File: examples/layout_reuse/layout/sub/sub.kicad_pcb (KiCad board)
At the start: 2 copper layers, 3 parts

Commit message: partialy fix simple val repr
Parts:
- R1, R2, R3: value {1000.0±1.0%}Ω -> 1000.0Ω
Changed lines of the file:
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@@
 			)
 		)
-		(property "Value" "{1000.0±1.0%}Ω"
+		(property "Value" "1000.0Ω"
 			(at 0 4)
 			(layer "F.Fab")
@@
 			(hide yes)
 		)
-		(property "resistance" "{1000.0±1.0%}Ω"
+		(property "resistance" "1000.0±1.0%Ω"
 			(at 0 0 0)
 			(layer "User.9")
@@
 			(hide yes)
 		)
-		(property "PARAM_resistance" "{\"type\": \"Quantity_Interval_Disjoint\", \"data\": {\"intervals\": {\"type\": \"Numeric_Interval_Disjoint\", \"data\": {\"intervals\": [{\"type\": \"Numeric_Interval\", \"data\": {\"min\": 990.0000002235174, \"max\": 1009.9999997764826}}]}}, \"unit\": \"\u03a9\"}}"
+		(property "PARAM_resistance" "{\"type\": \"Quantity_Interval_Disjoint\", \"data\": {\"intervals\": {\"type\": \"Numeric_Interval_Disjoint\", \"data\": {\"intervals\": [{\"type\": \"Numeric_Interval\", \"data\": {\"min\": 990.0000002235174, \"max\": 1009.9999997764826}}]}}, \"unit\": \"Ω\"}}"
 			(at 0 0 0)
 			(layer "User.9")
@@
 			)
 		)
-		(property "Value" "{1000.0±1.0%}Ω"
+		(property "Value" "1000.0Ω"
 			(at 0 4)
 			(layer "F.Fab")
@@
 			(hide yes)
 		)
-		(property "resistance" "{1000.0±1.0%}Ω"
+		(property "resistance" "1000.0±1.0%Ω"
 			(at 0 0 0)
 			(layer "User.9")
@@
 			(hide yes)
 		)
-		(property "PARAM_resistance" "{\"type\": \"Quantity_Interval_Disjoint\", \"data\": {\"intervals\": {\"type\": \"Numeric_Interval_Disjoint\", \"data\": {\"intervals\": [{\"type\": \"Numeric_Interval\", \"data\": {\"min\": 990.0000002235174, \"max\": 1009.9999997764826}}]}}, \"unit\": \"\u03a9\"}}"
+		(property "PARAM_resistance" "{\"type\": \"Quantity_Interval_Disjoint\", \"data\": {\"intervals\": {\"type\": \"Numeric_Interval_Disjoint\", \"data\": {\"intervals\": [{\"type\": \"Numeric_Interval\", \"data\": {\"min\": 990.0000002235174, \"max\": 1009.9999997764826}}]}}, \"unit\": \"Ω\"}}"
 			(at 0 0 0)
 			(layer "User.9")
@@
 			)
 		)
-		(property "Value" "{1000.0±1.0%}Ω"
+		(property "Value" "1000.0Ω"
 			(at 0 4)
 			(layer "F.Fab")
@@
 			(hide yes)
 		)
-		(property "resistance" "{1000.0±1.0%}Ω"
+		(property "resistance" "1000.0±1.0%Ω"
 			(at 0 0 0)
 			(layer "User.9")
@@
 			(hide yes)
 		)
-		(property "PARAM_resistance" "{\"type\": \"Quantity_Interval_Disjoint\", \"data\": {\"intervals\": {\"type\": \"Numeric_Interval_Disjoint\", \"data\": {\"intervals\": [{\"type\": \"Numeric_Interval\", \"data\": {\"min\": 990.0000002235174, \"max\": 1009.9999997764826}}]}}, \"unit\": \"\u03a9\"}}"
-			(at 0 0 0)
-			(layer "User.9")
+		(property "PARAM_resistance" "{\"type\": \"Quantity_Interval_Disjoint\", \"data\": {\"intervals\": {\"type\": \"Numeric_Interval_Disjoint\", \"data\": {\"intervals\": [{\"type\": \"Numeric_Interval\", \"data\": {\"min\": 990.0000002235174, \"max\": 1009.9999997764826}}]}}, \"unit\": \"Ω\"}}"
+			(at 0 0 0)
+			(layer "User.9")

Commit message: add builid
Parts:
- R1, R2, R3: value 1000.0Ω -> 1kΩ
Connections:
- net r_chain[0].unnamed[0]-unnamed[0] renamed unnamed[0]
- R1 pad 2: unnamed[0]-0 -> unnamed[0]-1
- R2 pad 1: unnamed[0]-0 -> unnamed[0]-1
- R2 pad 2: unnamed[0]-1 -> unnamed[0]-2
- R3 pad 1: unnamed[0]-1 -> unnamed[0]-2
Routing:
- net unnamed[0]-2: track 0.00 -> 1.57 mm
- net unnamed[0]-1: track 1.57 -> 0.00 mm
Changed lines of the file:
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@@
 			(usegerberadvancedattributes yes)
 			(creategerberjobfile yes)
-			(dashed_line_dash_ratio 12.000000)
-			(dashed_line_gap_ratio 3.000000)
+			(dashed_line_dash_ratio 12)
+			(dashed_line_gap_ratio 3)
 			(svgprecision 4)
 			(plotframeref no)
@@
 			(hpglpennumber 1)
 			(hpglpenspeed 20)
-			(hpglpendiameter 15.000000)
+			(hpglpendiameter 15)
 			(pdf_front_fp_property_popups yes)
 			(pdf_back_fp_property_popups yes)
@@
 	)
 	(net 1 "unnamed[1]")
-	(net 2 "unnamed[0]-1")
-	(net 3 "unnamed[0]-0")
-	(net 4 "r_chain[0].unnamed[0]-unnamed[0]")
+	(net 2 "unnamed[0]-2")
+	(net 3 "unnamed[0]-1")
+	(net 4 "unnamed[0]")
 	(footprint "UNI_ROYAL_0402WGF1001TCE:R0402"
 		(layer "F.Cu")
@@
 			)
 		)
-		(property "Value" "1000.0Ω"
+		(property "Value" "1kΩ"
 			(at 0 4)
 			(layer "F.Fab")
@@
 			(hide yes)
 		)
-		(property "resistance" "1000.0±1.0%Ω"
-			(at 0 0 0)
-			(layer "User.9")
-			(hide yes)
-		)
-		(property "max_power" "0.0625W"
-			(at 0 0 0)
-			(layer "User.9")
-			(hide yes)
-		)
-		(property "max_voltage" "50.0V"
+		(property "resistance" "1±20.0%kΩ"
+			(at 0 0 0)
+			(layer "User.9")
+			(hide yes)
+		)
+		(property "max_power" "any ≥0W"
+			(at 0 0 0)
+			(layer "User.9")
+			(hide yes)
+		)
+		(property "max_voltage" "any ≥0V"
 			(at 0 0 0)
 			(layer "User.9")
@@
 			(hide yes)
 		)
-		(property "PARAM_max_power" "{\"type\": \"Quantity_Set_Discrete\", \"data\": {\"intervals\": {\"type\": \"Numeric_Interval_Disjoint\", \"data\": {\"intervals\": [{\"type\": \"Numeric_Interval\", \"data\": {\"min\": 0.0625, \"max\": 0.0625}}]}}, \"unit\": \"W\"}}"
-			(at 0 0 0)
-			(layer "User.9")
-			(hide yes)
-		)
-		(property "PARAM_max_voltage" "{\"type\": \"Quantity_Set_Discrete\", \"data\": {\"intervals\": {\"type\": \"Numeric_Interval_Disjoint\", \"data\": {\"intervals\": [{\"type\": \"Numeric_Interval\", \"data\": {\"min\": 50.0, \"max\": 50.0}}]}}, \"unit\": \"V\"}}"
-			(at 0 0 0)
-			(layer "User.9")
-			(hide yes)
-		)
-		(property "PARAM_resistance" "{\"type\": \"Quantity_Interval_Disjoint\", \"data\": {\"intervals\": {\"type\": \"Numeric_Interval_Disjoint\", \"data\": {\"intervals\": [{\"type\": \"Numeric_Interval\", \"data\": {\"min\": 990.0000002235174, \"max\": 1009.9999997764826}}]}}, \"unit\": \"Ω\"}}"
+		(property "PARAM_max_power" "{\"type\": \"Quantity_Set_Discrete\", \"data\": {\"intervals\": {\"type\": \"Numeric_Interval_Disjoint\", \"data\": {\"intervals\": [{\"type\": \"Numeric_Interval\", \"data\": {\"min\": 0.0625, \"max\": 0.0625}}]}}, \"unit\": \"watt\"}}"
+			(at 0 0 0)
+			(layer "User.9")
+			(hide yes)
+		)
+		(property "PARAM_max_voltage" "{\"type\": \"Quantity_Set_Discrete\", \"data\": {\"intervals\": {\"type\": \"Numeric_Interval_Disjoint\", \"data\": {\"intervals\": [{\"type\": \"Numeric_Interval\", \"data\": {\"min\": 50.0, \"max\": 50.0}}]}}, \"unit\": \"volt\"}}"
+			(at 0 0 0)
+			(layer "User.9")
+			(hide yes)
+		)
+		(property "PARAM_resistance" "{\"type\": \"Quantity_Interval_Disjoint\", \"data\": {\"intervals\": {\"type\": \"Numeric_Interval_Disjoint\", \"data\": {\"intervals\": [{\"type\": \"Numeric_Interval\", \"data\": {\"min\": 990.0000002235174, \"max\": 1009.9999997764826}}]}}, \"unit\": \"ohm\"}}"
 			(at 0 0 0)
 			(layer "User.9")
@@
 			(size 0.57 0.54)
 			(layers "F.Cu" "F.Paste" "F.Mask")
-			(net 3 "unnamed[0]-0")
+			(net 3 "unnamed[0]-1")
 		)
 		(pad "1" smd rect
@@
 			(size 0.57 0.54)
 			(layers "F.Cu" "F.Paste" "F.Mask")
-			(net 4 "r_chain[0].unnamed[0]-unnamed[0]")
+			(net 4 "unnamed[0]")
 		)
 		(embedded_fonts no)
@@
 			)
 		)
-		(property "Value" "1000.0Ω"
+		(property "Value" "1kΩ"
 			(at 0 4)
 			(layer "F.Fab")
@@
 			(hide yes)
 		)
-		(property "resistance" "1000.0±1.0%Ω"
-			(at 0 0 0)
-			(layer "User.9")
-			(hide yes)
-		)
-		(property "max_power" "0.0625W"
-			(at 0 0 0)
-			(layer "User.9")
-			(hide yes)
-		)
-		(property "max_voltage" "50.0V"
+		(property "resistance" "1±20.0%kΩ"
+			(at 0 0 0)
+			(layer "User.9")
+			(hide yes)
+		)
+		(property "max_power" "any ≥0W"
+			(at 0 0 0)
+			(layer "User.9")
+			(hide yes)
+		)
+		(property "max_voltage" "any ≥0V"
 			(at 0 0 0)
 			(layer "User.9")
@@
 			(hide yes)
 		)
-		(property "PARAM_max_power" "{\"type\": \"Quantity_Set_Discrete\", \"data\": {\"intervals\": {\"type\": \"Numeric_Interval_Disjoint\", \"data\": {\"intervals\": [{\"type\": \"Numeric_Interval\", \"data\": {\"min\": 0.0625, \"max\": 0.0625}}]}}, \"unit\": \"W\"}}"
-			(at 0 0 0)
-			(layer "User.9")
-			(hide yes)
-		)
-		(property "PARAM_max_voltage" "{\"type\": \"Quantity_Set_Discrete\", \"data\": {\"intervals\": {\"type\": \"Numeric_Interval_Disjoint\", \"data\": {\"intervals\": [{\"type\": \"Numeric_Interval\", \"data\": {\"min\": 50.0, \"max\": 50.0}}]}}, \"unit\": \"V\"}}"
-			(at 0 0 0)
-			(layer "User.9")
-			(hide yes)
-		)
-		(property "PARAM_resistance" "{\"type\": \"Quantity_Interval_Disjoint\", \"data\": {\"intervals\": {\"type\": \"Numeric_Interval_Disjoint\", \"data\": {\"intervals\": [{\"type\": \"Numeric_Interval\", \"data\": {\"min\": 990.0000002235174, \"max\": 1009.9999997764826}}]}}, \"unit\": \"Ω\"}}"
+		(property "PARAM_max_power" "{\"type\": \"Quantity_Set_Discrete\", \"data\": {\"intervals\": {\"type\": \"Numeric_Interval_Disjoint\", \"data\": {\"intervals\": [{\"type\": \"Numeric_Interval\", \"data\": {\"min\": 0.0625, \"max\": 0.0625}}]}}, \"unit\": \"watt\"}}"
+			(at 0 0 0)
+			(layer "User.9")
+			(hide yes)
+		)
+		(property "PARAM_max_voltage" "{\"type\": \"Quantity_Set_Discrete\", \"data\": {\"intervals\": {\"type\": \"Numeric_Interval_Disjoint\", \"data\": {\"intervals\": [{\"type\": \"Numeric_Interval\", \"data\": {\"min\": 50.0, \"max\": 50.0}}]}}, \"unit\": \"volt\"}}"
+			(at 0 0 0)
+			(layer "User.9")
+			(hide yes)
+		)
+		(property "PARAM_resistance" "{\"type\": \"Quantity_Interval_Disjoint\", \"data\": {\"intervals\": {\"type\": \"Numeric_Interval_Disjoint\", \"data\": {\"intervals\": [{\"type\": \"Numeric_Interval\", \"data\": {\"min\": 990.0000002235174, \"max\": 1009.9999997764826}}]}}, \"unit\": \"ohm\"}}"
 			(at 0 0 0)
 			(layer "User.9")
@@
 			(size 0.57 0.54)
 			(layers "F.Cu" "F.Paste" "F.Mask")
-			(net 2 "unnamed[0]-1")
+			(net 2 "unnamed[0]-2")
 		)
 		(embedded_fonts no)
@@
 			)
 		)
-		(property "Value" "1000.0Ω"
+		(property "Value" "1kΩ"
 			(at 0 4)
 			(layer "F.Fab")
@@
 			(hide yes)
 		)
-		(property "resistance" "1000.0±1.0%Ω"
-			(at 0 0 0)
-			(layer "User.9")
-			(hide yes)
-		)
-		(property "max_power" "0.0625W"
-			(at 0 0 0)
-			(layer "User.9")
-			(hide yes)
-		)
-		(property "max_voltage" "50.0V"
+		(property "resistance" "1±20.0%kΩ"
+			(at 0 0 0)
+			(layer "User.9")
+			(hide yes)
+		)
+		(property "max_power" "any ≥0W"
+			(at 0 0 0)
+			(layer "User.9")
+			(hide yes)
+		)
+		(property "max_voltage" "any ≥0V"
 			(at 0 0 0)
 			(layer "User.9")
@@
 			(hide yes)
 		)
-		(property "PARAM_max_power" "{\"type\": \"Quantity_Set_Discrete\", \"data\": {\"intervals\": {\"type\": \"Numeric_Interval_Disjoint\", \"data\": {\"intervals\": [{\"type\": \"Numeric_Interval\", \"data\": {\"min\": 0.0625, \"max\": 0.0625}}]}}, \"unit\": \"W\"}}"
-			(at 0 0 0)
-			(layer "User.9")
-			(hide yes)
-		)
-		(property "PARAM_max_voltage" "{\"type\": \"Quantity_Set_Discrete\", \"data\": {\"intervals\": {\"type\": \"Numeric_Interval_Disjoint\", \"data\": {\"intervals\": [{\"type\": \"Numeric_Interval\", \"data\": {\"min\": 50.0, \"max\": 50.0}}]}}, \"unit\": \"V\"}}"
-			(at 0 0 0)
-			(layer "User.9")
-			(hide yes)
-		)
-		(property "PARAM_resistance" "{\"type\": \"Quantity_Interval_Disjoint\", \"data\": {\"intervals\": {\"type\": \"Numeric_Interval_Disjoint\", \"data\": {\"intervals\": [{\"type\": \"Numeric_Interval\", \"data\": {\"min\": 990.0000002235174, \"max\": 1009.9999997764826}}]}}, \"unit\": \"Ω\"}}"
+		(property "PARAM_max_power" "{\"type\": \"Quantity_Set_Discrete\", \"data\": {\"intervals\": {\"type\": \"Numeric_Interval_Disjoint\", \"data\": {\"intervals\": [{\"type\": \"Numeric_Interval\", \"data\": {\"min\": 0.0625, \"max\": 0.0625}}]}}, \"unit\": \"watt\"}}"
+			(at 0 0 0)
+			(layer "User.9")
+			(hide yes)
+		)
+		(property "PARAM_max_voltage" "{\"type\": \"Quantity_Set_Discrete\", \"data\": {\"intervals\": {\"type\": \"Numeric_Interval_Disjoint\", \"data\": {\"intervals\": [{\"type\": \"Numeric_Interval\", \"data\": {\"min\": 50.0, \"max\": 50.0}}]}}, \"unit\": \"volt\"}}"
+			(at 0 0 0)
+			(layer "User.9")
+			(hide yes)
+		)
+		(property "PARAM_resistance" "{\"type\": \"Quantity_Interval_Disjoint\", \"data\": {\"intervals\": {\"type\": \"Numeric_Interval_Disjoint\", \"data\": {\"intervals\": [{\"type\": \"Numeric_Interval\", \"data\": {\"min\": 990.0000002235174, \"max\": 1009.9999997764826}}]}}, \"unit\": \"ohm\"}}"
 			(at 0 0 0)
 			(layer "User.9")
@@
 			(size 0.57 0.54)
 			(layers "F.Cu" "F.Paste" "F.Mask")
-			(net 2 "unnamed[0]-1")
+			(net 2 "unnamed[0]-2")
 		)
 		(pad "1" smd rect
@@
 			(size 0.57 0.54)
 			(layers "F.Cu" "F.Paste" "F.Mask")
-			(net 3 "unnamed[0]-0")
+			(net 3 "unnamed[0]-1")
 		)
 		(embedded_fonts no)

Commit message: update layout_reuse layout and parts
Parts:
- R1, R2, R3: value 1kΩ -> 1000Ω
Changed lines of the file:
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@@
 	)
 	(setup
+		(stackup
+			(layer "F.SilkS"
+				(type "Top Silk Screen")
+			)
+			(layer "F.Paste"
+				(type "Top Solder Paste")
+			)
+			(layer "F.Mask"
+				(type "Top Solder Mask")
+				(color "Black")
+				(thickness 0.01)
+				(material "Solder mask")
+				(epsilon_r 3.3)
+			)
+			(layer "F.Cu"
+				(type "copper")
+				(thickness 0.035)
+			)
+			(layer "dielectric 1"
+				(type "core")
+				(thickness 1.51)
+				(material "FR4")
+				(epsilon_r 4.5)
+				(loss_tangent 0.02)
+			)
+			(layer "B.Cu"
+				(type "copper")
+				(thickness 0.035)
+			)
+			(layer "B.Mask"
+				(type "Bottom Solder Mask")
+				(color "Black")
+				(thickness 0.01)
+				(material "Solder mask")
+				(epsilon_r 3.3)
+			)
+			(layer "B.Paste"
+				(type "Bottom Solder Paste")
+			)
+			(layer "B.SilkS"
+				(type "Bottom Silk Screen")
+			)
+			(copper_finish "ENIG")
+		)
 		(pad_to_mask_clearance 0)
 		(allow_soldermask_bridges_in_footprints no)
@@
 			)
 		)
-		(property "Value" "1kΩ"
+		(property "Value" "1000Ω"
 			(at 0 4)
 			(layer "F.Fab")
@@
 			(hide yes)
 		)
-		(property "resistance" "1±20.0%kΩ"
-			(at 0 0 0)
-			(layer "User.9")
-			(hide yes)
-		)
-		(property "max_power" "any ≥0W"
-			(at 0 0 0)
-			(layer "User.9")
-			(hide yes)
-		)
-		(property "max_voltage" "any ≥0V"
+		(property "resistance" "1000±1.0%Ω"
+			(at 0 0 0)
+			(layer "User.9")
+			(hide yes)
+		)
+		(property "max_power" "0.062W"
+			(at 0 0 0)
+			(layer "User.9")
+			(hide yes)
+		)
+		(property "max_voltage" "50V"
 			(at 0 0 0)
 			(layer "User.9")
@@
 			)
 		)
-		(property "Value" "1kΩ"
+		(property "Value" "1000Ω"
 			(at 0 4)
 			(layer "F.Fab")
@@
 			(hide yes)
 		)
-		(property "resistance" "1±20.0%kΩ"
-			(at 0 0 0)
-			(layer "User.9")
-			(hide yes)
-		)
-		(property "max_power" "any ≥0W"
-			(at 0 0 0)
-			(layer "User.9")
-			(hide yes)
-		)
-		(property "max_voltage" "any ≥0V"
+		(property "resistance" "1000±1.0%Ω"
+			(at 0 0 0)
+			(layer "User.9")
+			(hide yes)
+		)
+		(property "max_power" "0.062W"
+			(at 0 0 0)
+			(layer "User.9")
+			(hide yes)
+		)
+		(property "max_voltage" "50V"
 			(at 0 0 0)
 			(layer "User.9")
@@
 			)
 		)
-		(property "Value" "1kΩ"
+		(property "Value" "1000Ω"
 			(at 0 4)
 			(layer "F.Fab")
@@
 			(hide yes)
 		)
-		(property "resistance" "1±20.0%kΩ"
-			(at 0 0 0)
-			(layer "User.9")
-			(hide yes)
-		)
-		(property "max_power" "any ≥0W"
-			(at 0 0 0)
-			(layer "User.9")
-			(hide yes)
-		)
-		(property "max_voltage" "any ≥0V"
-			(at 0 0 0)
-			(layer "User.9")
+		(property "resistance" "1000±1.0%Ω"
+			(at 0 0 0)
+			(layer "User.9")
+			(hide yes)
+		)
+		(property "max_power" "0.062W"
+			(at 0 0 0)
+			(layer "User.9")
+			(hide yes)
+		)
+		(property "max_voltage" "50V"
+			(at 0 0 0)
+			(layer "User.9")

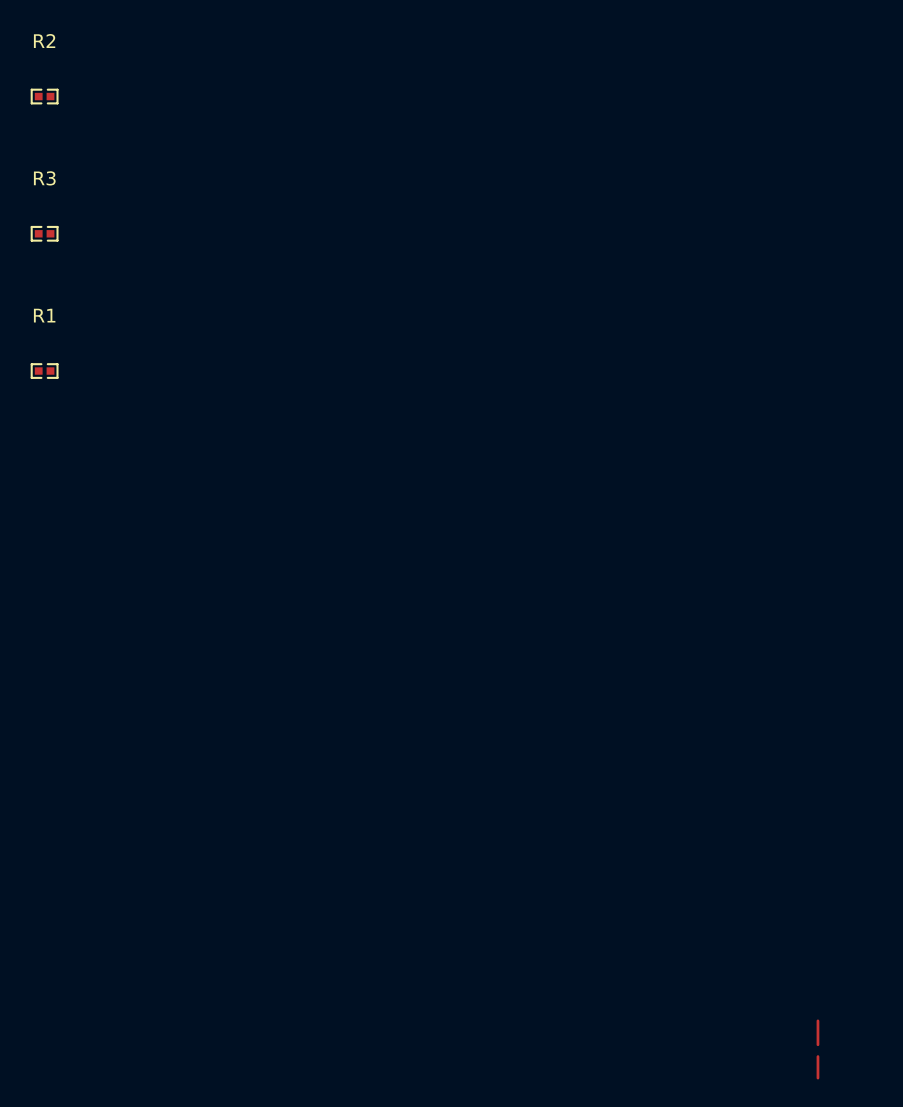
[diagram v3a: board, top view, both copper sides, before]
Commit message: Examples: update examples (#1769)
- simpler I2C example
- fix led badge builds
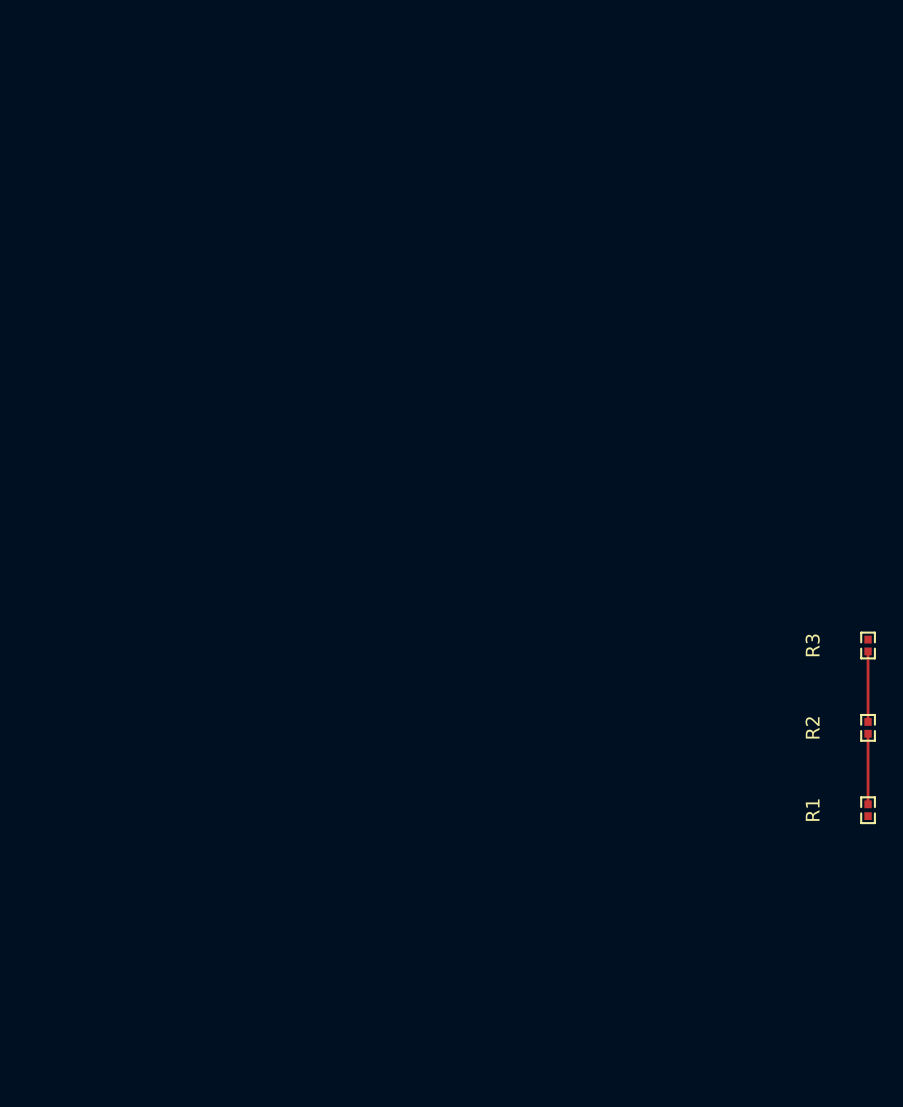
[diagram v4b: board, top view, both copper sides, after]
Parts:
- R1, R2, R3: value 1000Ω -> 1kΩ
- moved R2 75.6 mm to (60.0, 26.0), turned to 90 degrees
- moved R1 68.0 mm to (60.0, 32.0), turned to 90 degrees
- moved R3 67.1 mm to (60.0, 20.0), turned to 90 degrees
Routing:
- net unnamed[0]-1: track 0.00 -> 5.14 mm
- net unnamed[0]-2: track 1.57 -> 5.14 mm
- net unnamed[0]: track 1.74 -> 0.00 mm
